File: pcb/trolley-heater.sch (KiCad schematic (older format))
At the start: 44 parts, among them K1 RELAY_SPDT, K2 RELAY_SPDT, K3 RELAY_SPDT, K4 RELAY_SPDT, K5 RELAY_SPDT, K6 RELAY_SPDT, P1 CONN_01X03, P10 CONN_01X02, P2 CONN_01X03, P3 CONN_01X03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

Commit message: updated: prepare for 1.0 release.
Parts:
- renumbered P9 to P10, P10 to P8, P8 to P9
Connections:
- net at K2.11 (C1): now also P6.1 (P1); no longer P6.2 (P2)
- net at K2.14 (T1): now also P6.2 (P2); no longer P6.1 (P1)
- net at K4.11 (C1): now also P8.1 (P1); no longer P8.2 (P2)
- net at K4.14 (T1): now also P8.2 (P2); no longer P8.1 (P1)
- net at K1.11 (C1): now also P5.1 (P1); no longer P5.2 (P2)
- net at K1.14 (T1): now also P5.2 (P2); no longer P5.1 (P1)
- net at K6.11 (C1): now also P10.1 (P1); no longer P10.2 (P2)
- net at K6.14 (T1): now also P10.2 (P2); no longer P10.1 (P1)
- net at K3.11 (C1): now also P7.1 (P1); no longer P7.2 (P2)
- net at K3.14 (T1): now also P7.2 (P2); no longer P7.1 (P1)
- net at K5.11 (C1): now also P9.1 (P1); no longer P9.2 (P2)
- net at K5.14 (T1): now also P9.2 (P2); no longer P9.1 (P1)
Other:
- moved on the sheet: P8
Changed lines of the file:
@@
 	12900 3950 13100 3950
 Connection ~ 13100 3950
-Wire Wire Line
-	13900 1900 14050 1900
-Wire Wire Line
-	13900 2000 14050 2000
-Wire Wire Line
-	14050 2100 13900 2100
 Text Label 2500 3250 0    60   ~ 0
 CH1_IN
@@
 F 3 "" H 12300 2050 50  0000 C CNN
 	1    12300 2050
-	1    0    0    1
-$EndComp
-$Comp
-L CONN_01X02 P10
+	1    0    0    -1
+$EndComp
+$Comp
+L CONN_01X02 P8
 U 1 1 57AB2497
-P 14250 2050
-F 0 "P10" H 14250 2200 50  0000 C CNN
-F 1 "CONN_01X02" V 14350 2050 50  0000 C CNN
-F 2 "Terminal_Blocks:TerminalBlock_Pheonix_MKDS1.5-2pol" H 14250 2050 50  0001 C CNN
-F 3 "" H 14250 2050 50  0000 C CNN
-	1    14250 2050
-	1    0    0    1
+P 14100 2050
+F 0 "P8" H 14100 2200 50  0000 C CNN
+F 1 "CONN_01X02" V 14200 2050 50  0000 C CNN
+F 2 "Terminal_Blocks:TerminalBlock_Pheonix_MKDS1.5-2pol" H 14100 2050 50  0001 C CNN
+F 3 "" H 14100 2050 50  0000 C CNN
+	1    14100 2050
+	1    0    0    -1
 $EndComp
 $Comp
@@
 F 3 "" H 12300 3650 50  0000 C CNN
 	1    12300 3650
-	1    0    0    1
-$EndComp
-$Comp
-L CONN_01X02 P8
+	1    0    0    -1
+$EndComp
+$Comp
+L CONN_01X02 P9
 U 1 1 57AB2622
 P 14100 3650
-F 0 "P8" H 14100 3800 50  0000 C CNN
+F 0 "P9" H 14100 3800 50  0000 C CNN
 F 1 "CONN_01X02" V 14200 3650 50  0000 C CNN
 F 2 "Terminal_Blocks:TerminalBlock_Pheonix_MKDS1.5-2pol" H 14100 3650 50  0001 C CNN
 F 3 "" H 14100 3650 50  0000 C CNN
 	1    14100 3650
-	1    0    0    1
+	1    0    0    -1
 $EndComp
 $Comp
@@
 F 3 "" H 12300 5300 50  0000 C CNN
 	1    12300 5300
-	1    0    0    1
-$EndComp
-$Comp
-L CONN_01X02 P9
+	1    0    0    -1
+$EndComp
+$Comp
+L CONN_01X02 P10
 U 1 1 57AB27CF
 P 14100 5300
-F 0 "P9" H 14100 5450 50  0000 C CNN
+F 0 "P10" H 14100 5450 50  0000 C CNN
 F 1 "CONN_01X02" V 14200 5300 50  0000 C CNN
 F 2 "Terminal_Blocks:TerminalBlock_Pheonix_MKDS1.5-2pol" H 14100 5300 50  0001 C CNN
 F 3 "" H 14100 5300 50  0000 C CNN
 	1    14100 5300
-	1    0    0    1
+	1    0    0    -1
 $EndComp
 NoConn ~ 12100 1900
-NoConn ~ 14050 1900
+NoConn ~ 13900 1900
 NoConn ~ 12100 3500
 NoConn ~ 13900 3500

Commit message: updated: with fill and additional mains filtering.
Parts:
- added F1: 0.8A, components:Fuse_Radial, symbol F_Small
- added V1: 275V, Varistors:RV_Disc_D12_W5_P7.5, symbol VR
- R1, R2, R3, R4, R5, R6: footprint Resistors_ThroughHole:Resistor_Horizontal_RM10mm -> Resistors_ThroughHole:Resistor_Vertical_RM5mm
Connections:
- net +5V: now also U4.3 (-Vo); no longer U4.4 (+Vo)
- net GNDREF: now also U4.4 (+Vo); no longer U4.3 (-Vo)
- net at P4.1 (P1), U4.2 (AC): now also V1.2
- net at P4.2 (P2): now also F1.1; no longer U4.1 (AC)
- new net: F1.2, U4.1 (AC), V1.1
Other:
- moved on the sheet: P4
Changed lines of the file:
@@
 L CONN_01X02 P4
 U 1 1 57A8DFC3
-P 6100 2850
-F 0 "P4" H 6100 3000 50  0000 C CNN
-F 1 "CONN_01X02" V 6200 2850 50  0000 C CNN
-F 2 "Terminal_Blocks:TerminalBlock_Pheonix_MKDS1.5-2pol" H 6100 2850 50  0001 C CNN
-F 3 "" H 6100 2850 50  0000 C CNN
-	1    6100 2850
-	-1   0    0    -1
+P 5400 2850
+F 0 "P4" H 5400 3000 50  0000 C CNN
+F 1 "CONN_01X02" V 5500 2850 50  0000 C CNN
+F 2 "Terminal_Blocks:TerminalBlock_Pheonix_MKDS1.5-2pol" H 5400 2850 50  0001 C CNN
+F 3 "" H 5400 2850 50  0000 C CNN
+	1    5400 2850
+	-1   0    0    1
 $EndComp
 $Comp
@@
 F 0 "R1" V 2180 3500 50  0000 C CNN
 F 1 "2k2" V 2100 3500 50  0000 C CNN
-F 2 "Resistors_ThroughHole:Resistor_Horizontal_RM10mm" V 2030 3500 50  0001 C CNN
+F 2 "Resistors_ThroughHole:Resistor_Vertical_RM5mm" V 2030 3500 50  0001 C CNN
 F 3 "" H 2100 3500 50  0000 C CNN
 	1    2100 3500
@@
 F 0 "R4" V 2430 3250 50  0000 C CNN
 F 1 "1k" V 2350 3250 50  0000 C CNN
-F 2 "Resistors_ThroughHole:Resistor_Horizontal_RM10mm" V 2280 3250 50  0001 C CNN
+F 2 "Resistors_ThroughHole:Resistor_Vertical_RM5mm" V 2280 3250 50  0001 C CNN
 F 3 "" H 2350 3250 50  0000 C CNN
 	1    2350 3250
@@
 F 0 "R2" V 2180 4700 50  0000 C CNN
 F 1 "2k2" V 2100 4700 50  0000 C CNN
-F 2 "Resistors_ThroughHole:Resistor_Horizontal_RM10mm" V 2030 4700 50  0001 C CNN
+F 2 "Resistors_ThroughHole:Resistor_Vertical_RM5mm" V 2030 4700 50  0001 C CNN
 F 3 "" H 2100 4700 50  0000 C CNN
 	1    2100 4700
@@
 F 0 "R5" V 2430 4450 50  0000 C CNN
 F 1 "1k" V 2350 4450 50  0000 C CNN
-F 2 "Resistors_ThroughHole:Resistor_Horizontal_RM10mm" V 2280 4450 50  0001 C CNN
+F 2 "Resistors_ThroughHole:Resistor_Vertical_RM5mm" V 2280 4450 50  0001 C CNN
 F 3 "" H 2350 4450 50  0000 C CNN
 	1    2350 4450
@@
 F 0 "R3" V 2180 5900 50  0000 C CNN
 F 1 "2k2" V 2100 5900 50  0000 C CNN
-F 2 "Resistors_ThroughHole:Resistor_Horizontal_RM10mm" V 2030 5900 50  0001 C CNN
+F 2 "Resistors_ThroughHole:Resistor_Vertical_RM5mm" V 2030 5900 50  0001 C CNN
 F 3 "" H 2100 5900 50  0000 C CNN
 	1    2100 5900
@@
 F 0 "R6" V 2430 5650 50  0000 C CNN
 F 1 "1k" V 2350 5650 50  0000 C CNN
-F 2 "Resistors_ThroughHole:Resistor_Horizontal_RM10mm" V 2280 5650 50  0001 C CNN
+F 2 "Resistors_ThroughHole:Resistor_Vertical_RM5mm" V 2280 5650 50  0001 C CNN
 F 3 "" H 2350 5650 50  0000 C CNN
 	1    2350 5650
@@
 F 3 "http://www.hlktech.net/product_detail.php?ProId=54" H 6900 2850 60  0001 C CNN
 	1    6900 2850
-	1    0    0    1
+	1    0    0    -1
 $EndComp
 Wire Wire Line
@@
 Wire Wire Line
 	7400 2750 7400 2650
-Wire Wire Line
-	6300 2800 6300 2750
-Wire Wire Line
-	6300 2750 6500 2750
-Wire Wire Line
-	6300 2900 6300 2950
-Wire Wire Line
-	6300 2950 6500 2950
 Connection ~ 7400 2750
+$Comp
+L VR V1
+U 1 1 5886B76F
+P 6200 2850
+F 0 "V1" V 6260 2804 50  0000 C TNN
+F 1 "275V" V 6200 2850 50  0000 C CNN
+F 2 "Varistors:RV_Disc_D12_W5_P7.5" H 6200 2850 50  0001 C CNN
+F 3 "http://www.farnell.com/datasheets/1899727.pdf" H 6200 2850 50  0001 C CNN
+	1    6200 2850
+	1    0    0    -1
+$EndComp
+$Comp
+L F_Small F1
+U 1 1 5886B7DE
+P 5900 2600
+F 0 "F1" H 5860 2660 50  0000 L CNN
+F 1 "0.8A" H 5780 2540 50  0000 L CNN
+F 2 "components:Fuse_Radial" H 5900 2600 50  0001 C CNN
+F 3 "http://www.farnell.com/datasheets/1662441.pdf" H 5900 2600 50  0001 C CNN
+	1    5900 2600
+	1    0    0    -1
+$EndComp
+Wire Wire Line
+	6500 2600 6500 2750
+Wire Wire Line
+	6000 2600 6500 2600
+Wire Wire Line
+	6500 3100 6500 2950
+Wire Wire Line
+	5600 3100 6500 3100
+Connection ~ 6200 2600
+Wire Wire Line
+	5600 2800 5600 2600
+Wire Wire Line
+	5600 2600 5800 2600
+Wire Wire Line
+	5600 3100 5600 2900
+Connection ~ 6200 3100
 $EndSCHEMATC

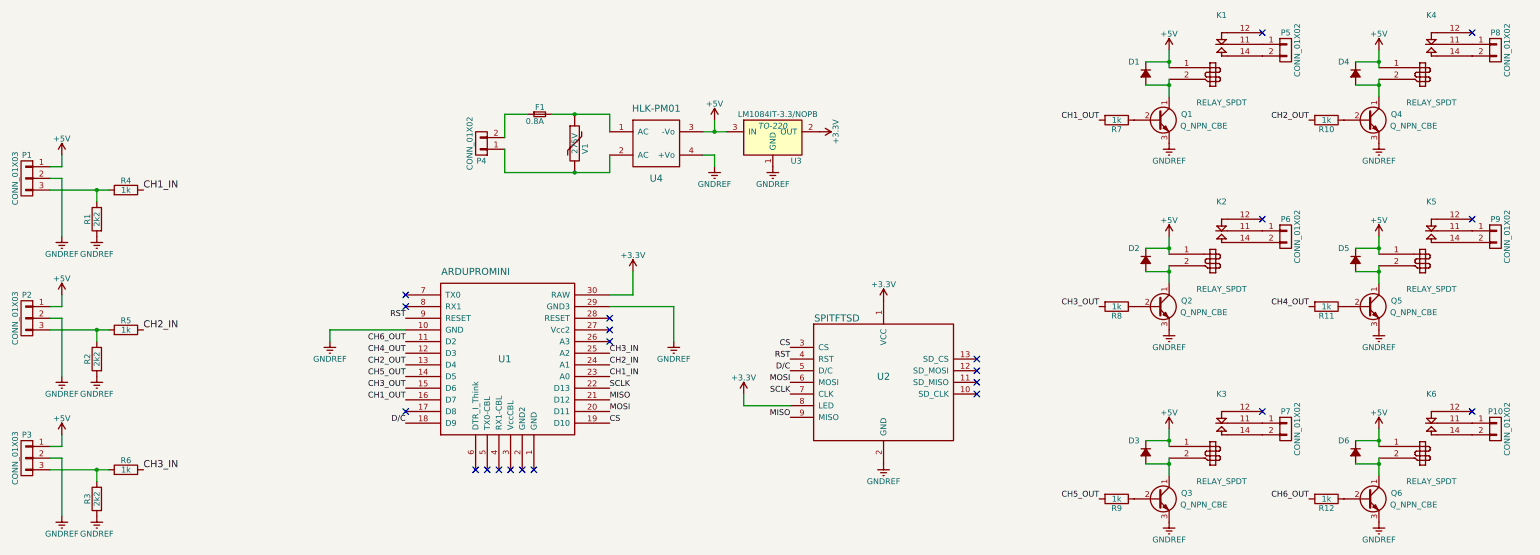
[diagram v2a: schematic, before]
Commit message: updated: tweaking ac input connector and battery pack support.
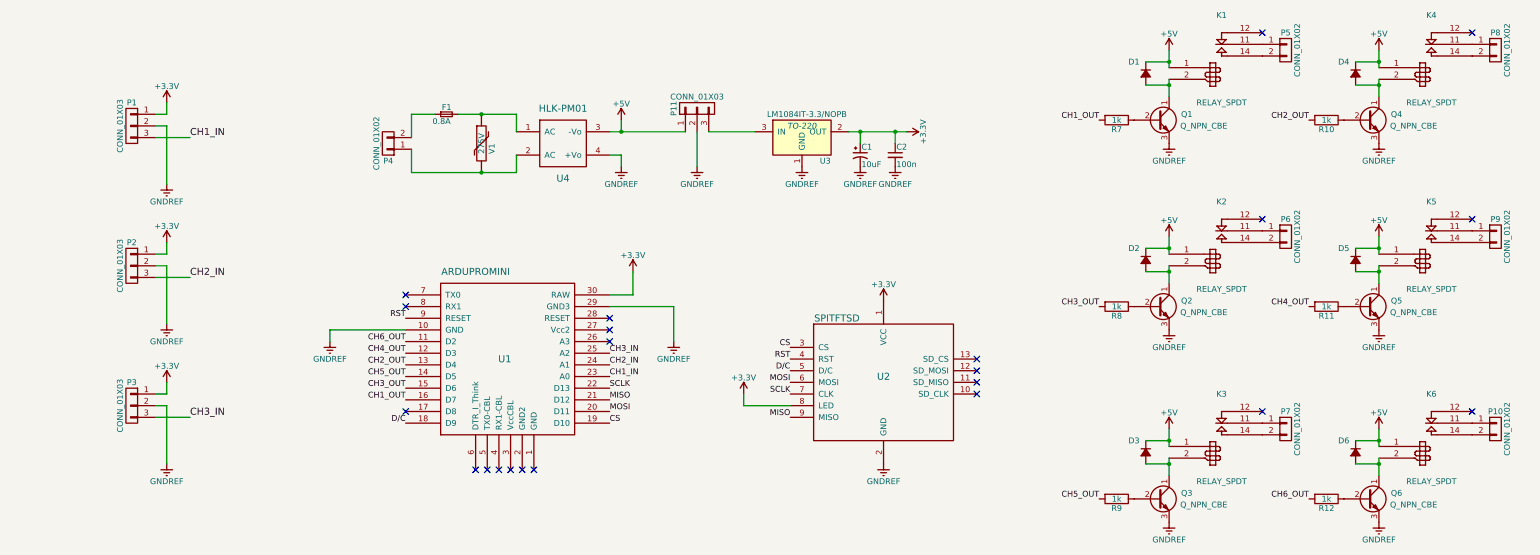
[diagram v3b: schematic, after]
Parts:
- removed R1, R2, R3: 2k2, Resistors_ThroughHole:Resistor_Vertical_RM5mm, symbol R
- removed R4, R5, R6: 1k, Resistors_ThroughHole:Resistor_Vertical_RM5mm, symbol R
- added C1: 10uF, Capacitors_ThroughHole:C_Radial_D10_L13_P5, symbol CP1_Small
- added C2: 100n, symbol C_Small
- added P11: CONN_01X03, Pin_Headers:Pin_Header_Straight_1x03, symbol CONN_01X03
- P10, P5, P6, P7, P8, P9: footprint Terminal_Blocks:TerminalBlock_Pheonix_MKDS1.5-2pol -> components:TerminalBlock_Pheonix_PT-5.08mm_2pol
- P4: footprint Terminal_Blocks:TerminalBlock_Pheonix_MKDS1.5-2pol -> components:TerminalBlock_Pheonix_PT-7.5mm_2pol
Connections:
- net +3V3: now also P1.1 (P1), P2.1 (P1), P3.1 (P1), C1.1, C2.1
- net +5V: now also P11.1 (P1); no longer P1.1 (P1), P2.1 (P1), P3.1 (P1), U3.3 (IN)
- net CH1_IN: now also P1.3 (P3)
- net CH2_IN: now also P2.3 (P3)
- net CH3_IN: now also P3.3 (P3)
- net GNDREF: now also C1.2, C2.2, P11.2 (P2)
- new net: P11.3 (P3), U3.3 (IN)
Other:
- moved on the sheet: F1, P1, P2, P3, P4, U3, U4, V1
